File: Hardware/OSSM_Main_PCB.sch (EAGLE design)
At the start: 9 parts, among them J1 PJ-037AH, U1 LOLIN32_PRODUCTION

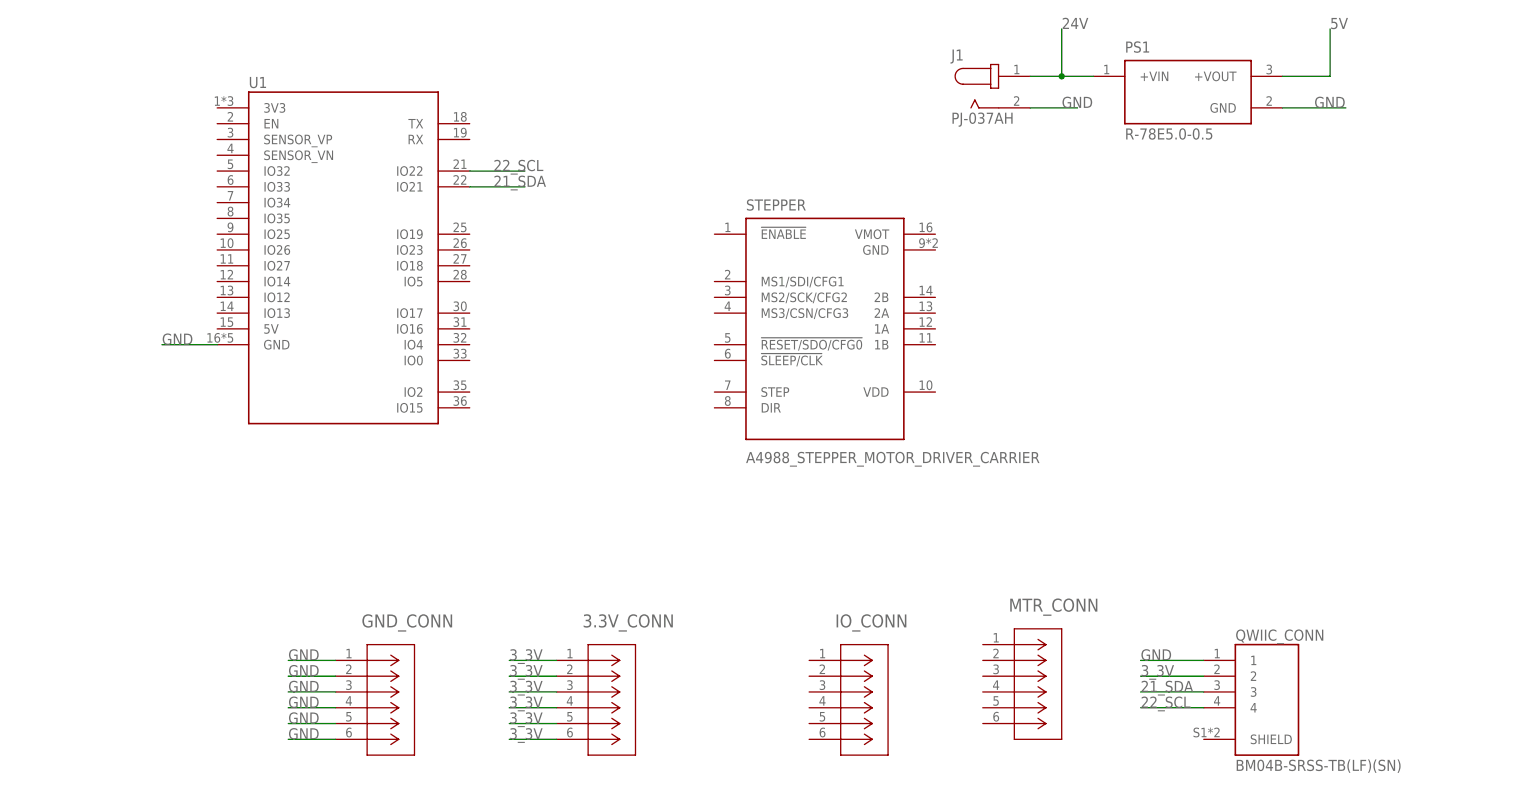
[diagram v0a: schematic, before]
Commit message: Added Diode on 5V regulator
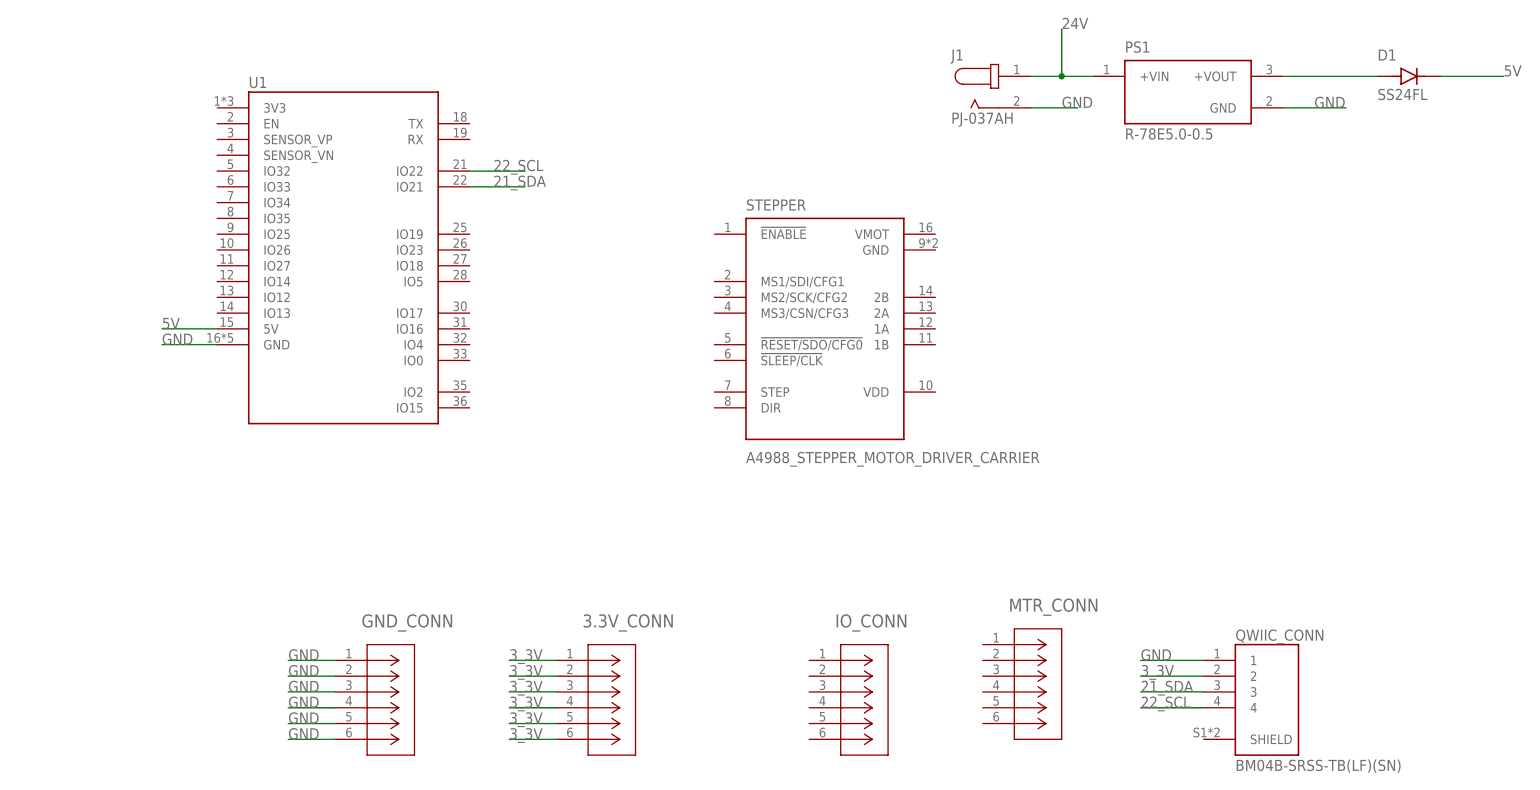
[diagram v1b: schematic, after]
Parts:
- added D1: SS24FL, SS24FL:SS24FL
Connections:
- new net N$1: D1.A, PS1.+VOUT
- net 5V: now also D1.C, U1.5V; no longer PS1.+VOUT
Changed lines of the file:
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@@
 <part name="J1" library="PJ-037AH" deviceset="PJ-037AH" device=""/>
 <part name="PS1" library="R-78E5.0-0.5" deviceset="R-78E5.0-0.5" device=""/>
+<part name="D1" library="SS24FL" deviceset="SS24FL" device=""/>
 </parts>
 <sheets>
@@
 <attribute name="NAME" x="182.8761" y="163.8379" size="1.77938125" layer="95"/>
 <attribute name="VALUE" x="182.8786" y="149.8573" size="1.77848125" layer="96"/>
+</instance>
+<instance part="D1" gate="G$1" x="228.6" y="160.02" smashed="yes">
+<attribute name="NAME" x="223.52" y="162.56" size="1.778" layer="95"/>
+<attribute name="VALUE" x="223.52" y="156.21" size="1.778" layer="96"/>
 </instance>
 </instances>
@@
 </segment>
 </net>
+<net name="N$1" class="0">
+<segment>
+<pinref part="PS1" gate="G$1" pin="+VOUT"/>
+<pinref part="D1" gate="G$1" pin="A"/>
+<wire x1="208.28" y1="160.02" x2="223.52" y2="160.02" width="0.1524" layer="91"/>
+</segment>
+</net>
 <net name="5V" class="0">
 <segment>
-<pinref part="PS1" gate="G$1" pin="+VOUT"/>
-<wire x1="208.28" y1="160.02" x2="215.9" y2="160.02" width="0.1524" layer="91"/>
-<wire x1="215.9" y1="160.02" x2="215.9" y2="167.64" width="0.1524" layer="91"/>
-<label x="215.9" y="167.64" size="1.778" layer="95"/>
+<pinref part="D1" gate="G$1" pin="C"/>
+<wire x1="233.68" y1="160.02" x2="243.84" y2="160.02" width="0.1524" layer="91"/>
+<label x="243.84" y="160.02" size="1.778" layer="95"/>
+</segment>
+<segment>
+<pinref part="U1" gate="G$1" pin="5V"/>
+<wire x1="36.83" y1="119.38" x2="27.94" y2="119.38" width="0.1524" layer="91"/>
+<label x="27.94" y="119.38" size="1.778" layer="95"/>
 </segment>
 </net>

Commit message: James' Attempt
Maybe made it better, maybe made it worse?
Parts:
- added C1: (no value), rcl:C-US050-024X044
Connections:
- new net N$10: MTR_CONN.4, STEPPER.2A
- new net N$11: MTR_CONN.3, STEPPER.2B
- new net N$12: IO_CONN.1, U1.IO12
- new net N$13: IO_CONN.2, U1.IO14
- new net N$14: IO_CONN.3, U1.IO27
- new net N$15: IO_CONN.4, U1.IO26
- new net N$16: IO_CONN.5, U1.IO25
- new net N$17: IO_CONN.6, U1.IO35
- new net N$2: STEPPER.!ENABLE, U1.IO19
- new net N$3: STEPPER.MS1/SDI/CFG1, U1.IO23
- new net N$4: STEPPER.MS2/SCK/CFG2, U1.IO18
- new net N$5: STEPPER.MS3/CSN/CFG3, U1.IO17
- new net N$6: STEPPER.STEP, U1.IO16
- new net N$7: STEPPER.DIR, U1.IO13
- new net N$8: MTR_CONN.6, STEPPER.1B
- new net N$9: MTR_CONN.5, STEPPER.1A
- net 24V: now also C1.2, STEPPER.VMOT
- net 5V: now also STEPPER.VDD
- net GND: now also C1.1, STEPPER.GND
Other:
- moved on the sheet: IO_CONN, MTR_CONN
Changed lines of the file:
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@@
 <?xml version="1.0" encoding="utf-8"?>
 <!DOCTYPE eagle SYSTEM "eagle.dtd">
-<eagle version="9.6.1">
+<eagle version="9.6.2">
 <drawing>
 <settings>
@@
 <part name="PS1" library="R-78E5.0-0.5" deviceset="R-78E5.0-0.5" device=""/>
 <part name="D1" library="SS24FL" deviceset="SS24FL" device=""/>
+<part name="C1" library="rcl" library_urn="urn:adsk.eagle:library:334" deviceset="C-US" device="050-024X044" package3d_urn="urn:adsk.eagle:package:23643/1"/>
 </parts>
 <sheets>
@@
 <attribute name="NAME" x="95.6056" y="71.3486" size="2.0828" layer="95" ratio="6" rot="SR0"/>
 </instance>
-<instance part="IO_CONN" gate="A" x="132.08" y="66.04" smashed="yes">
-<attribute name="NAME" x="136.2456" y="71.3486" size="2.0828" layer="95" ratio="6" rot="SR0"/>
-</instance>
-<instance part="MTR_CONN" gate="A" x="160.02" y="68.58" smashed="yes">
-<attribute name="NAME" x="164.1856" y="73.8886" size="2.0828" layer="95" ratio="6" rot="SR0"/>
+<instance part="IO_CONN" gate="A" x="22.86" y="124.46" smashed="yes" rot="R180">
+<attribute name="NAME" x="18.6944" y="119.1514" size="2.0828" layer="95" ratio="6" rot="SR180"/>
+</instance>
+<instance part="MTR_CONN" gate="A" x="187.96" y="129.54" smashed="yes">
+<attribute name="NAME" x="192.1256" y="134.8486" size="2.0828" layer="95" ratio="6" rot="SR0"/>
 </instance>
 <instance part="QWIIC_CONN" gate="G$1" x="205.74" y="58.42" smashed="yes">
@@
 <attribute name="NAME" x="223.52" y="162.56" size="1.778" layer="95"/>
 <attribute name="VALUE" x="223.52" y="156.21" size="1.778" layer="96"/>
+</instance>
+<instance part="C1" gate="G$1" x="160.02" y="144.78" smashed="yes" rot="R270">
+<attribute name="NAME" x="160.655" y="143.764" size="1.778" layer="95" rot="R270"/>
+<attribute name="VALUE" x="155.829" y="143.764" size="1.778" layer="96" rot="R270"/>
 </instance>
 </instances>
@@
 <wire x1="167.64" y1="154.94" x2="175.26" y2="154.94" width="0.1524" layer="91"/>
 <label x="172.72" y="154.94" size="1.778" layer="95"/>
+<pinref part="STEPPER" gate="G$1" pin="GND"/>
+<wire x1="152.4" y1="132.08" x2="167.64" y2="132.08" width="0.1524" layer="91"/>
+<wire x1="167.64" y1="132.08" x2="167.64" y2="144.78" width="0.1524" layer="91"/>
+<junction x="167.64" y="154.94"/>
+<pinref part="C1" gate="G$1" pin="1"/>
+<wire x1="167.64" y1="144.78" x2="167.64" y2="154.94" width="0.1524" layer="91"/>
+<wire x1="162.56" y1="144.78" x2="167.64" y2="144.78" width="0.1524" layer="91"/>
+<junction x="167.64" y="144.78"/>
 </segment>
 <segment>
@@
 <label x="172.72" y="167.64" size="1.778" layer="95"/>
 </segment>
+<segment>
+<pinref part="STEPPER" gate="G$1" pin="VMOT"/>
+<wire x1="152.4" y1="134.62" x2="154.94" y2="134.62" width="0.1524" layer="91"/>
+<wire x1="154.94" y1="134.62" x2="157.48" y2="134.62" width="0.1524" layer="91"/>
+<wire x1="157.48" y1="134.62" x2="160.02" y2="134.62" width="0.1524" layer="91"/>
+<label x="160.02" y="134.62" size="1.778" layer="95"/>
+<pinref part="C1" gate="G$1" pin="2"/>
+<wire x1="154.94" y1="144.78" x2="154.94" y2="134.62" width="0.1524" layer="91"/>
+<junction x="154.94" y="134.62"/>
+</segment>
 </net>
 <net name="N$1" class="0">
@@
 <wire x1="36.83" y1="119.38" x2="27.94" y2="119.38" width="0.1524" layer="91"/>
 <label x="27.94" y="119.38" size="1.778" layer="95"/>
+</segment>
+<segment>
+<pinref part="STEPPER" gate="G$1" pin="VDD"/>
+<wire x1="152.4" y1="109.22" x2="160.02" y2="109.22" width="0.1524" layer="91"/>
+<label x="162.56" y="109.22" size="1.778" layer="95"/>
+</segment>
+</net>
+<net name="N$2" class="0">
+<segment>
+<pinref part="U1" gate="G$1" pin="IO19"/>
+<pinref part="STEPPER" gate="G$1" pin="!ENABLE"/>
+<wire x1="77.47" y1="134.62" x2="116.84" y2="134.62" width="0.1524" layer="91"/>
+</segment>
+</net>
+<net name="N$3" class="0">
+<segment>
+<pinref part="U1" gate="G$1" pin="IO23"/>
+<wire x1="77.47" y1="132.08" x2="104.14" y2="132.08" width="0.1524" layer="91"/>
+<wire x1="104.14" y1="132.08" x2="106.68" y2="132.08" width="0.1524" layer="91"/>
+<wire x1="106.68" y1="132.08" x2="106.68" y2="129.54" width="0.1524" layer="91"/>
+<pinref part="STEPPER" gate="G$1" pin="MS1/SDI/CFG1"/>
+<wire x1="106.68" y1="129.54" x2="106.68" y2="127" width="0.1524" layer="91"/>
+<wire x1="106.68" y1="127" x2="116.84" y2="127" width="0.1524" layer="91"/>
+</segment>
+</net>
+<net name="N$4" class="0">
+<segment>
+<pinref part="U1" gate="G$1" pin="IO18"/>
+<wire x1="77.47" y1="129.54" x2="104.14" y2="129.54" width="0.1524" layer="91"/>
+<wire x1="104.14" y1="129.54" x2="104.14" y2="124.46" width="0.1524" layer="91"/>
+<pinref part="STEPPER" gate="G$1" pin="MS2/SCK/CFG2"/>
+<wire x1="104.14" y1="124.46" x2="116.84" y2="124.46" width="0.1524" layer="91"/>
+</segment>
+</net>
+<net name="N$5" class="0">
+<segment>
+<pinref part="U1" gate="G$1" pin="IO17"/>
+<pinref part="STEPPER" gate="G$1" pin="MS3/CSN/CFG3"/>
+<wire x1="77.47" y1="121.92" x2="116.84" y2="121.92" width="0.1524" layer="91"/>
+</segment>
+</net>
+<net name="N$6" class="0">
+<segment>
+<pinref part="U1" gate="G$1" pin="IO16"/>
+<wire x1="77.47" y1="119.38" x2="106.68" y2="119.38" width="0.1524" layer="91"/>
+<pinref part="STEPPER" gate="G$1" pin="STEP"/>
+<wire x1="106.68" y1="119.38" x2="106.68" y2="109.22" width="0.1524" layer="91"/>
+<wire x1="106.68" y1="109.22" x2="116.84" y2="109.22" width="0.1524" layer="91"/>
+</segment>
+</net>
+<net name="N$7" class="0">
+<segment>
+<pinref part="U1" gate="G$1" pin="IO13"/>
+<wire x1="36.83" y1="121.92" x2="25.4" y2="121.92" width="0.1524" layer="91"/>
+<wire x1="25.4" y1="121.92" x2="25.4" y2="99.06" width="0.1524" layer="91"/>
+<wire x1="25.4" y1="99.06" x2="111.76" y2="99.06" width="0.1524" layer="91"/>
+<pinref part="STEPPER" gate="G$1" pin="DIR"/>
+<wire x1="111.76" y1="99.06" x2="116.84" y2="99.06" width="0.1524" layer="91"/>
+<wire x1="116.84" y1="99.06" x2="116.84" y2="106.68" width="0.1524" layer="91"/>
+</segment>
+</net>
+<net name="N$8" class="0">
+<segment>
+<pinref part="STEPPER" gate="G$1" pin="1B"/>
+<pinref part="MTR_CONN" gate="A" pin="6"/>
+<wire x1="152.4" y1="116.84" x2="187.96" y2="116.84" width="0.1524" layer="91"/>
+</segment>
+</net>
+<net name="N$9" class="0">
+<segment>
+<pinref part="MTR_CONN" gate="A" pin="5"/>
+<pinref part="STEPPER" gate="G$1" pin="1A"/>
+<wire x1="187.96" y1="119.38" x2="152.4" y2="119.38" width="0.1524" layer="91"/>
+</segment>
+</net>
+<net name="N$10" class="0">
+<segment>
+<pinref part="STEPPER" gate="G$1" pin="2A"/>
+<pinref part="MTR_CONN" gate="A" pin="4"/>
+<wire x1="152.4" y1="121.92" x2="187.96" y2="121.92" width="0.1524" layer="91"/>
+</segment>
+</net>
+<net name="N$11" class="0">
+<segment>
+<pinref part="MTR_CONN" gate="A" pin="3"/>
+<pinref part="STEPPER" gate="G$1" pin="2B"/>
+<wire x1="187.96" y1="124.46" x2="152.4" y2="124.46" width="0.1524" layer="91"/>
+</segment>
+</net>
+<net name="N$12" class="0">
+<segment>
+<pinref part="U1" gate="G$1" pin="IO12"/>
+<pinref part="IO_CONN" gate="A" pin="1"/>
+<wire x1="36.83" y1="124.46" x2="22.86" y2="124.46" width="0.1524" layer="91"/>
+</segment>
+</net>
+<net name="N$13" class="0">
+<segment>
+<pinref part="IO_CONN" gate="A" pin="2"/>
+<pinref part="U1" gate="G$1" pin="IO14"/>
+<wire x1="22.86" y1="127" x2="36.83" y2="127" width="0.1524" layer="91"/>
+</segment>
+</net>
+<net name="N$14" class="0">
+<segment>
+<pinref part="U1" gate="G$1" pin="IO27"/>
+<pinref part="IO_CONN" gate="A" pin="3"/>
+<wire x1="36.83" y1="129.54" x2="22.86" y2="129.54" width="0.1524" layer="91"/>
+</segment>
+</net>
+<net name="N$15" class="0">
+<segment>
+<pinref part="IO_CONN" gate="A" pin="4"/>
+<pinref part="U1" gate="G$1" pin="IO26"/>
+<wire x1="22.86" y1="132.08" x2="36.83" y2="132.08" width="0.1524" layer="91"/>
+</segment>
+</net>
+<net name="N$16" class="0">
+<segment>
+<pinref part="U1" gate="G$1" pin="IO25"/>
+<pinref part="IO_CONN" gate="A" pin="5"/>
+<wire x1="36.83" y1="134.62" x2="22.86" y2="134.62" width="0.1524" layer="91"/>
+</segment>
+</net>
+<net name="N$17" class="0">
+<segment>
+<pinref part="IO_CONN" gate="A" pin="6"/>
+<pinref part="U1" gate="G$1" pin="IO35"/>
+<wire x1="22.86" y1="137.16" x2="36.83" y2="137.16" width="0.1524" layer="91"/>
 </segment>
 </net>
@@
 will not be understood (or retained) with this version.
 </note>
+<note version="8.3" severity="warning">
+Since Version 8.3, EAGLE supports the association of 3D packages
+with devices in libraries, schematics, and board files. Those 3D
+packages will not be understood (or retained) with this version.
+</note>
+<note version="8.4" severity="warning">
+Since Version 8.4, EAGLE supports properties for SPICE simulation.
+Probes in schematics and SPICE mapping objects found in parts and library devices
+will not be understood with this version. Update EAGLE to the latest version
+for full support of SPICE simulation.
+</note>
 </compatibility>

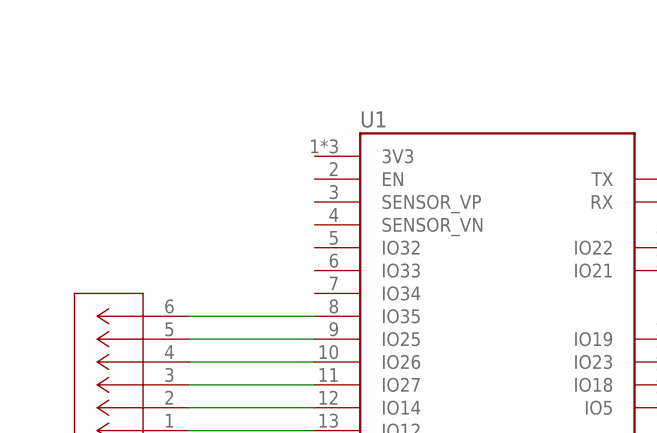
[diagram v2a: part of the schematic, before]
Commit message: beefed up ground, added PCB ground
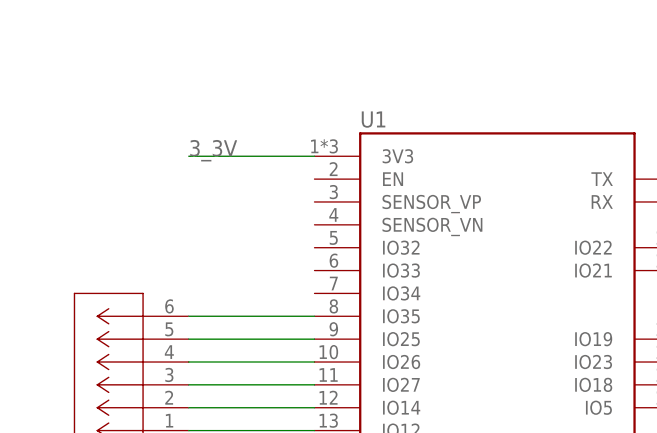
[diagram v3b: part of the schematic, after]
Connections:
- net 3_3V: now also U1.3V3
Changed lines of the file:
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@@
 <label x="185.42" y="63.5" size="1.778" layer="95"/>
+</segment>
+<segment>
+<pinref part="U1" gate="G$1" pin="3V3"/>
+<wire x1="36.83" y1="154.94" x2="22.86" y2="154.94" width="0.1524" layer="91"/>
+<label x="22.86" y="154.94" size="1.778" layer="95"/>
 </segment>
 </net>
